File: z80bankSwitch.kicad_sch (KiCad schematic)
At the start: 27 parts, among them J1 Conn_02x05_Odd_Even, P101 CONN_01X04, P102 CONN_02X20, U1 SST39SF040, U101 7400, U102 Z8400, U105 74LS138, U2 AS6C4008-55PCN, Y101 4MHz

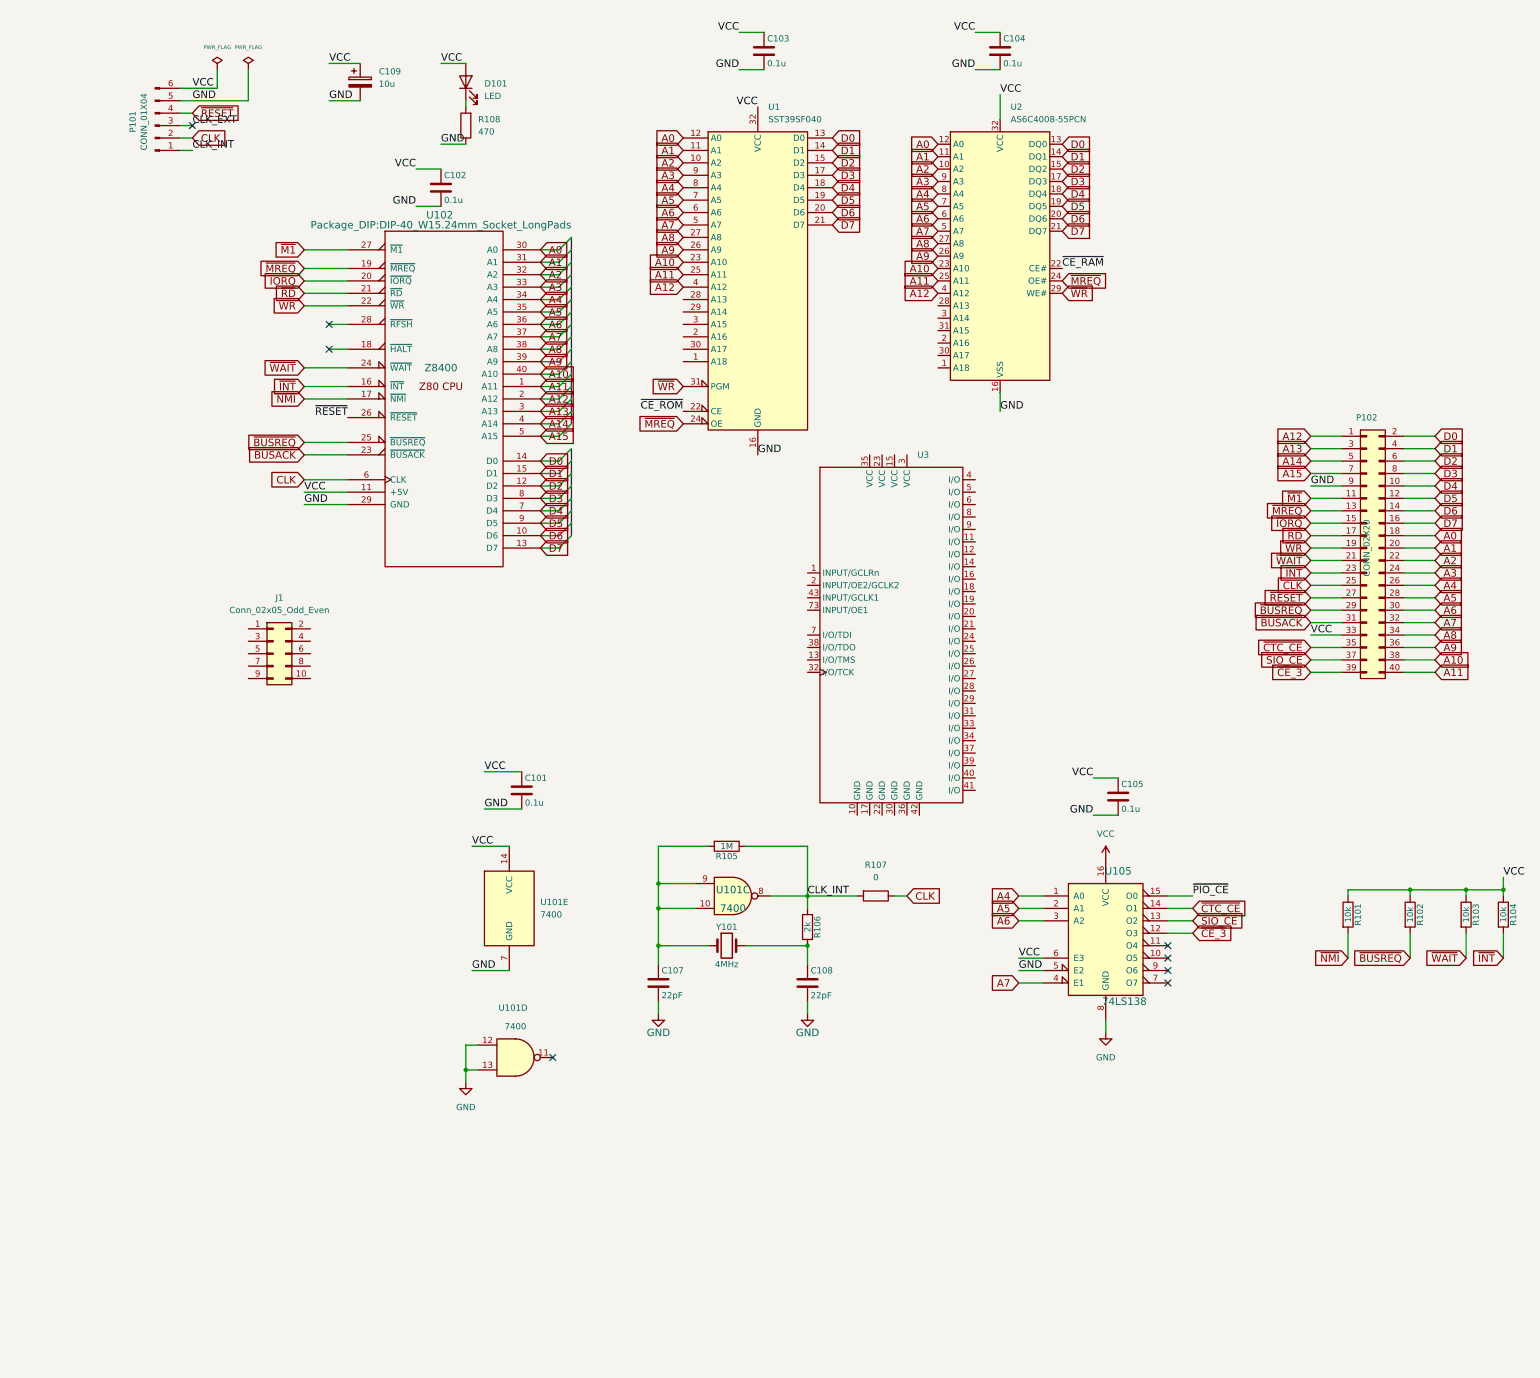
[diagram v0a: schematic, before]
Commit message: Use Z80 from global own library instead
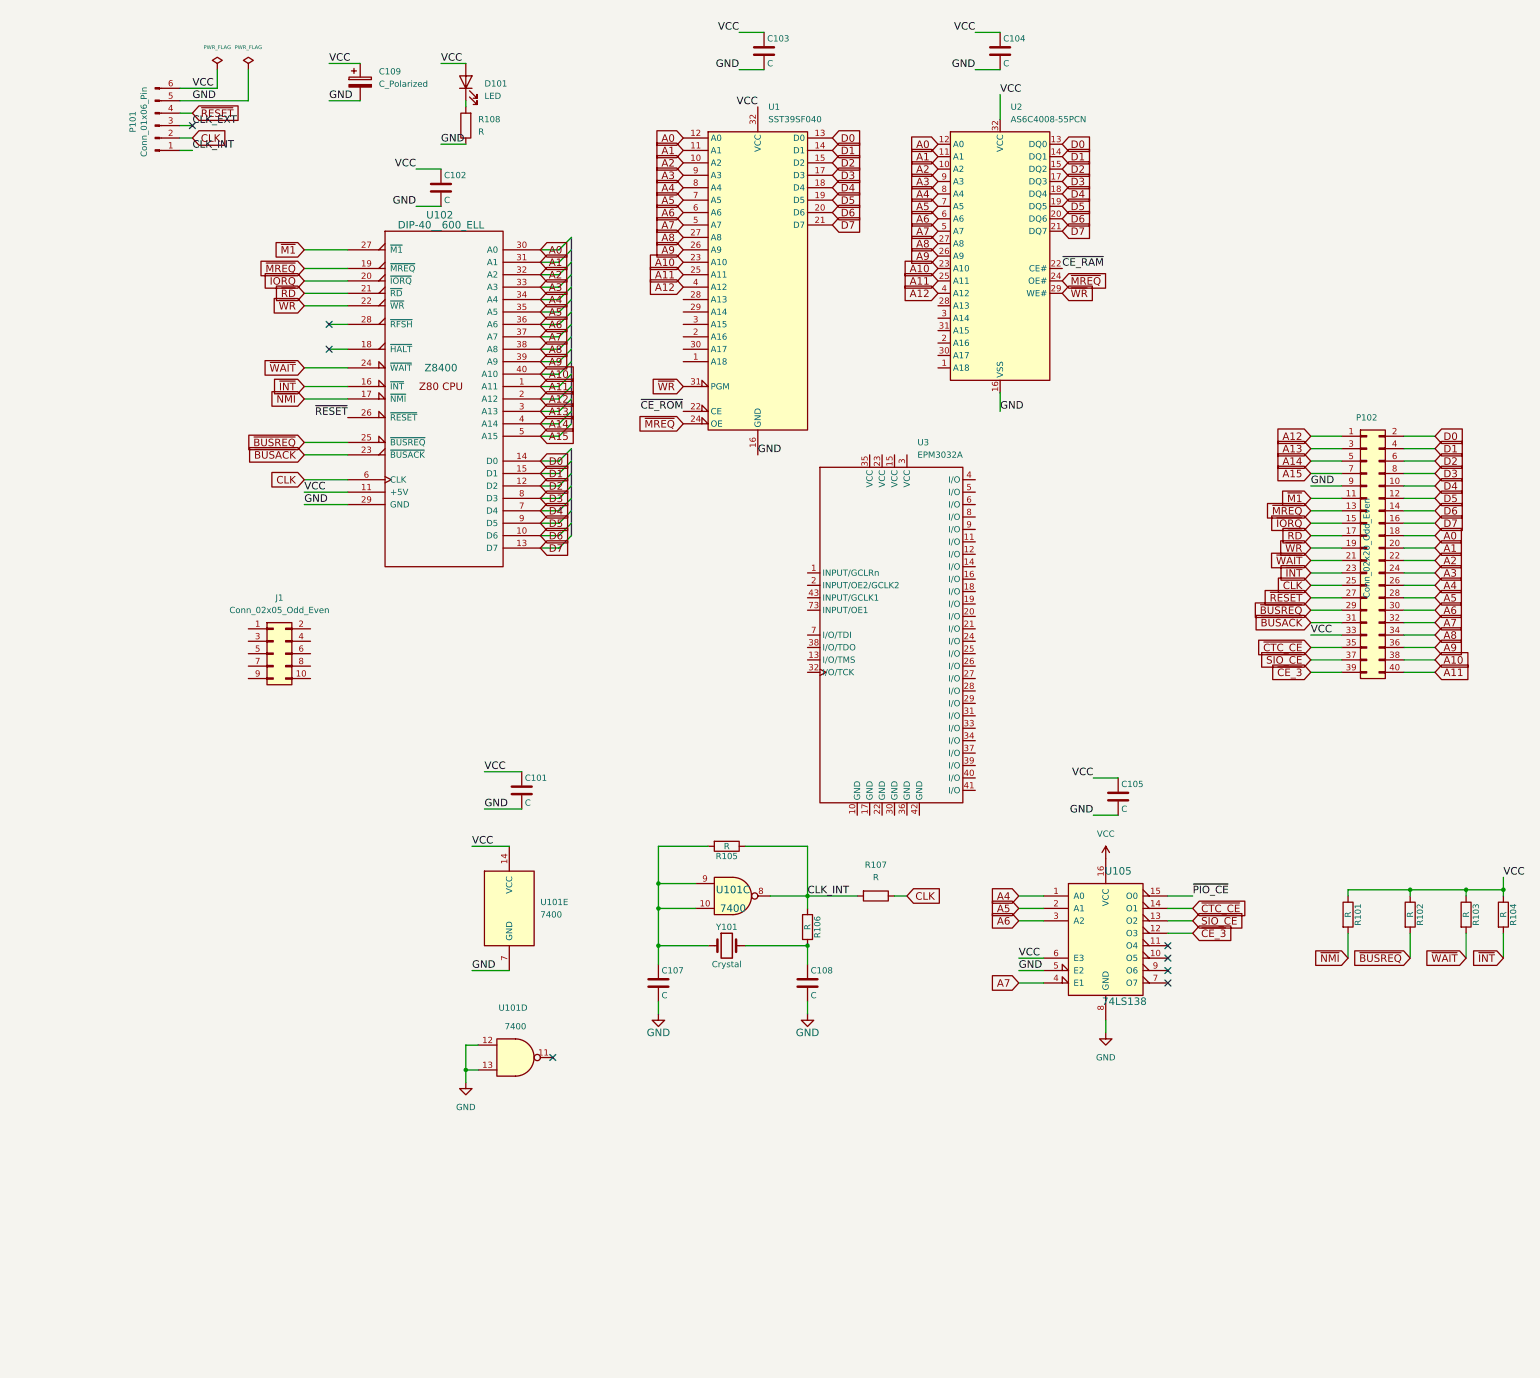
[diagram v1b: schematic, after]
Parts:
- C101, C102, C103, C104, C105: value 0.1u -> C
- C107, C108: value 22pF -> C
- C109: value 10u -> C_Polarized
- P101: value CONN_01X04 -> Conn_01x06_Pin
- P102: value CONN_02X20 -> Conn_02x20_Odd_Even
- R101, R102, R103, R104: value 10k -> R
- R105: value 1M -> R
- R106: value 2k -> R
- R107: value 0 -> R
- R108: value 470 -> R
- U102: footprint Package_DIP:DIP-40_W15.24mm_Socket_LongPads -> DIP-40__600_ELL; symbol z80-ownSymbols:Z8400 -> Own Symbol Library:Z8400
- U2: footprint Package_SO:TSOP-I-32_18.4x8mm_P0.5mm -> Package_DIP:DIP-32_W15.24mm
- U3: value (none) -> EPM3032A
- Y101: value 4MHz -> Crystal
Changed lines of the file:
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@@
 	)
 	(symbol
-		(lib_id "z80-ownSymbols:Z8400")
+		(lib_id "Own Symbol Library:Z8400")
 		(at 102.87 92.71 0)
 		(unit 1)
@@
 			)
 		)
-		(property "Footprint" "Package_DIP:DIP-40_W15.24mm_Socket_LongPads"
+		(property "Footprint" "DIP-40__600_ELL"
 			(at 101.6 58.42 0)
 			(show_name no)
@@
 		)
 		(instances
-			(project "z80"
+			(project "z80bankSwitch"
 				(path "/e7eeb274-d662-49f9-a7ce-d4911c9f2b64"
 					(reference "U102")
@@
 		)
 		(instances
-			(project "z80"
+			(project "z80bankSwitch"
 				(path "/e7eeb274-d662-49f9-a7ce-d4911c9f2b64"
 					(reference "U105")
@@
 			)
 		)
-		(property "Value" "CONN_01X04"
+		(property "Value" "Conn_01x06_Pin"
 			(at 40.894 37.338 90)
 			(show_name no)
@@
 		)
 		(instances
-			(project "z80"
+			(project "z80bankSwitch"
 				(path "/e7eeb274-d662-49f9-a7ce-d4911c9f2b64"
 					(reference "P101")
@@
 		)
 		(instances
-			(project "z80"
+			(project "z80bankSwitch"
 				(path "/e7eeb274-d662-49f9-a7ce-d4911c9f2b64"
 					(reference "#FLG0101")
@@
 		)
 		(instances
-			(project "z80"
+			(project "z80bankSwitch"
 				(path "/e7eeb274-d662-49f9-a7ce-d4911c9f2b64"
 					(reference "#FLG0102")
@@
 			)
 		)
-		(property "Value" "CONN_02X20"
+		(property "Value" "Conn_02x20_Odd_Even"
 			(at 290.83 124.46 90)
 			(show_name no)
@@
 		)
 		(instances
-			(project "z80"
+			(project "z80bankSwitch"
 				(path "/e7eeb274-d662-49f9-a7ce-d4911c9f2b64"
 					(reference "P102")
@@
 			)
 		)
-		(property "Value" "10k"
+		(property "Value" "R"
 			(at 318.77 199.39 90)
 			(show_name no)
@@
 		)
 		(instances
-			(project "z80"
+			(project "z80bankSwitch"
 				(path "/e7eeb274-d662-49f9-a7ce-d4911c9f2b64"
 					(reference "R104")
@@
 			)
 		)
-		(property "Value" "0.1u"
+		(property "Value" "C"
 			(at 118.745 176.53 0)
 			(show_name no)
@@
 		)
 		(instances
-			(project "z80"
+			(project "z80bankSwitch"
 				(path "/e7eeb274-d662-49f9-a7ce-d4911c9f2b64"
 					(reference "C101")
@@
 			)
 		)
-		(property "Value" "0.1u"
+		(property "Value" "C"
 			(at 102.235 53.34 0)
 			(show_name no)
@@
 		)
 		(instances
-			(project "z80"
+			(project "z80bankSwitch"
 				(path "/e7eeb274-d662-49f9-a7ce-d4911c9f2b64"
 					(reference "C102")
@@
 			)
 		)
-		(property "Value" "0.1u"
+		(property "Value" "C"
 			(at 168.275 25.4 0)
 			(show_name no)
@@
 		)
 		(instances
-			(project "z80"
+			(project "z80bankSwitch"
 				(path "/e7eeb274-d662-49f9-a7ce-d4911c9f2b64"
 					(reference "C103")
@@
 			)
 		)
-		(property "Value" "0.1u"
+		(property "Value" "C"
 			(at 216.535 25.4 0)
 			(show_name no)
@@
 		)
 		(instances
-			(project "z80"
+			(project "z80bankSwitch"
 				(path "/e7eeb274-d662-49f9-a7ce-d4911c9f2b64"
 					(reference "C104")
@@
 			)
 		)
-		(property "Value" "0.1u"
+		(property "Value" "C"
 			(at 240.665 177.8 0)
 			(show_name no)
@@
 		)
 		(instances
-			(project "z80"
+			(project "z80bankSwitch"
 				(path "/e7eeb274-d662-49f9-a7ce-d4911c9f2b64"
 					(reference "C105")
@@
 		)
 		(instances
-			(project "z80"
+			(project "z80bankSwitch"
 				(path "/e7eeb274-d662-49f9-a7ce-d4911c9f2b64"
 					(reference "U101")
@@
 			)
 		)
-		(property "Value" "2k"
+		(property "Value" "R"
 			(at 176.53 201.93 90)
 			(show_name no)
@@
 		)
 		(instances
-			(project "z80"
+			(project "z80bankSwitch"
 				(path "/e7eeb274-d662-49f9-a7ce-d4911c9f2b64"
 					(reference "R106")
@@
 			)
 		)
-		(property "Value" "22pF"
+		(property "Value" "C"
 			(at 177.165 215.9 0)
 			(show_name no)
@@
 		)
 		(instances
-			(project "z80"
+			(project "z80bankSwitch"
 				(path "/e7eeb274-d662-49f9-a7ce-d4911c9f2b64"
 					(reference "C108")
@@
 			)
 		)
-		(property "Value" "22pF"
+		(property "Value" "C"
 			(at 146.685 215.9 0)
 			(show_name no)
@@
 		)
 		(instances
-			(project "z80"
+			(project "z80bankSwitch"
 				(path "/e7eeb274-d662-49f9-a7ce-d4911c9f2b64"
 					(reference "C107")
@@
 			)
 		)
-		(property "Value" "4MHz"
+		(property "Value" "Crystal"
 			(at 160.02 209.55 0)
 			(show_name no)
@@
 		)
 		(instances
-			(project "z80"
+			(project "z80bankSwitch"
 				(path "/e7eeb274-d662-49f9-a7ce-d4911c9f2b64"
 					(reference "Y101")
@@
 			)
 		)
-		(property "Value" "1M"
+		(property "Value" "R"
 			(at 160.02 185.42 90)
 			(show_name no)
@@
 		)
 		(instances
-			(project "z80"
+			(project "z80bankSwitch"
 				(path "/e7eeb274-d662-49f9-a7ce-d4911c9f2b64"
 					(reference "R105")
@@
 		)
 		(instances
-			(project "z80"
+			(project "z80bankSwitch"
 				(path "/e7eeb274-d662-49f9-a7ce-d4911c9f2b64"
 					(reference "#PWR0102")
@@
 		)
 		(instances
-			(project "z80"
+			(project "z80bankSwitch"
 				(path "/e7eeb274-d662-49f9-a7ce-d4911c9f2b64"
 					(reference "#PWR0101")
@@
 		)
 		(instances
-			(project "z80"
+			(project "z80bankSwitch"
 				(path "/e7eeb274-d662-49f9-a7ce-d4911c9f2b64"
 					(reference "#PWR0105")
@@
 			)
 		)
-		(property "Value" "0"
+		(property "Value" "R"
 			(at 190.5 191.77 90)
 			(show_name no)
@@
 		)
 		(instances
-			(project "z80"
+			(project "z80bankSwitch"
 				(path "/e7eeb274-d662-49f9-a7ce-d4911c9f2b64"
 					(reference "R107")
@@
 		)
 		(instances
-			(project "z80"
+			(project "z80bankSwitch"
 				(path "/e7eeb274-d662-49f9-a7ce-d4911c9f2b64"
 					(reference "#PWR0104")
@@
 		)
 		(instances
-			(project "z80"
+			(project "z80bankSwitch"
 				(path "/e7eeb274-d662-49f9-a7ce-d4911c9f2b64"
 					(reference "U101")
@@
 		)
 		(instances
-			(project "z80"
+			(project "z80bankSwitch"
 				(path "/e7eeb274-d662-49f9-a7ce-d4911c9f2b64"
 					(reference "U1")
@@
 		(fields_autoplaced yes)
 		(property "Reference" "U3"
-			(at 198.9933 105.41 0)
+			(at 198.9933 102.87 0)
 			(show_name no)
 			(do_not_autoplace no)
@@
 			)
 		)
-		(property "Value" ""
-			(at 193.04 138.43 0)
+		(property "Value" "EPM3032A"
+			(at 198.9933 105.41 0)
 			(show_name no)
 			(do_not_autoplace no)
@@
 					(size 1.27 1.27)
 				)
+				(justify left)
 			)
 		)
@@
 		)
 		(instances
-			(project "z80"
+			(project "z80bankSwitch"
 				(path "/e7eeb274-d662-49f9-a7ce-d4911c9f2b64"
 					(reference "U3")
@@
 		)
 		(instances
-			(project "z80"
+			(project "z80bankSwitch"
 				(path "/e7eeb274-d662-49f9-a7ce-d4911c9f2b64"
 					(reference "J1")
@@
 			)
 		)
-		(property "Value" "10u"
+		(property "Value" "C_Polarized"
 			(at 88.9 29.5909 0)
 			(show_name no)
@@
 		)
 		(instances
-			(project "z80"
+			(project "z80bankSwitch"
 				(path "/e7eeb274-d662-49f9-a7ce-d4911c9f2b64"
 					(reference "C109")
@@
 		)
 		(instances
-			(project "z80"
+			(project "z80bankSwitch"
 				(path "/e7eeb274-d662-49f9-a7ce-d4911c9f2b64"
 					(reference "#PWR0103")
@@
 			)
 		)
-		(property "Value" "10k"
+		(property "Value" "R"
 			(at 311.15 199.39 90)
 			(show_name no)
@@
 		)
 		(instances
-			(project "z80"
+			(project "z80bankSwitch"
 				(path "/e7eeb274-d662-49f9-a7ce-d4911c9f2b64"
 					(reference "R103")
@@
 		)
 		(instances
-			(project "z80"
+			(project "z80bankSwitch"
 				(path "/e7eeb274-d662-49f9-a7ce-d4911c9f2b64"
 					(reference "U101")
@@
 		)
 		(instances
-			(project "z80"
+			(project "z80bankSwitch"
 				(path "/e7eeb274-d662-49f9-a7ce-d4911c9f2b64"
 					(reference "D101")
@@
 			)
 		)
-		(property "Value" "10k"
+		(property "Value" "R"
 			(at 287.02 199.39 90)
 			(show_name no)
@@
 		)
 		(instances
-			(project "z80"
+			(project "z80bankSwitch"
 				(path "/e7eeb274-d662-49f9-a7ce-d4911c9f2b64"
 					(reference "R101")
@@
 			)
 		)
-		(property "Value" "10k"
+		(property "Value" "R"
 			(at 299.72 199.39 90)
 			(show_name no)
@@
 		)
 		(instances
-			(project "z80"
+			(project "z80bankSwitch"
 				(path "/e7eeb274-d662-49f9-a7ce-d4911c9f2b64"
 					(reference "R102")
@@
 			)
 		)
-		(property "Value" "470"
+		(property "Value" "R"
 			(at 109.22 39.3699 0)
 			(show_name no)
@@
 		)
 		(instances
-			(project "z80"
+			(project "z80bankSwitch"
 				(path "/e7eeb274-d662-49f9-a7ce-d4911c9f2b64"
 					(reference "R108")
@@
 			)
 		)
-		(property "Footprint" "Package_SO:TSOP-I-32_18.4x8mm_P0.5mm"
+		(property "Footprint" "Package_DIP:DIP-32_W15.24mm"
 			(at 215.9 62.23 0)
 			(hide yes)
@@
 		)
 		(instances
-			(project "z80"
+			(project "z80bankSwitch"
 				(path "/e7eeb274-d662-49f9-a7ce-d4911c9f2b64"
 					(reference "U2")

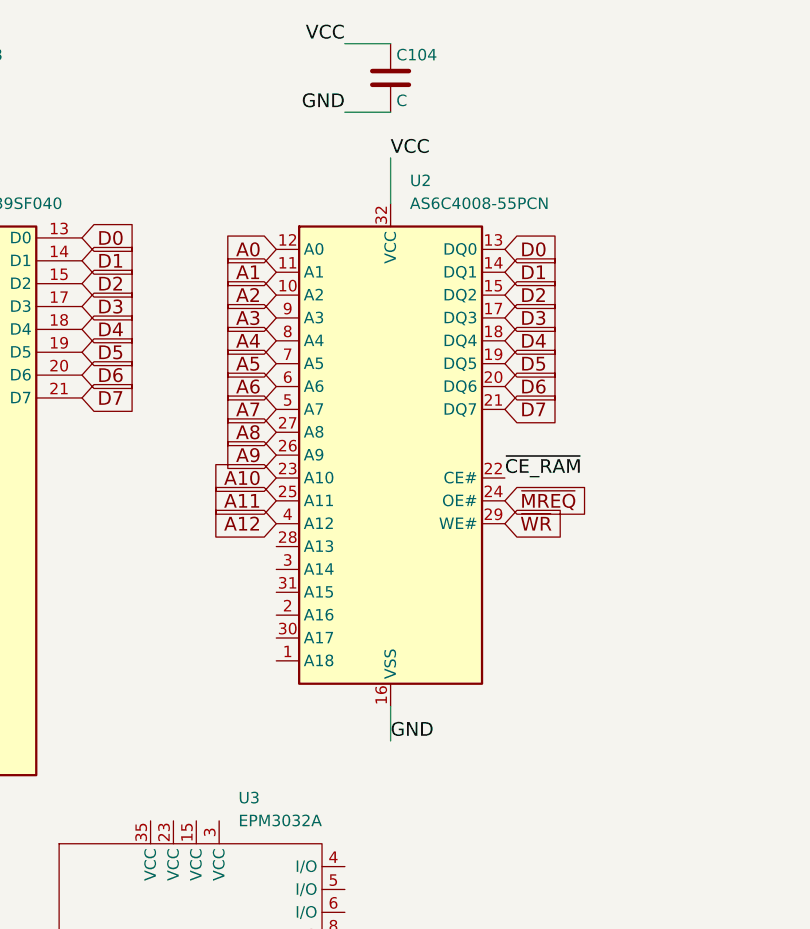
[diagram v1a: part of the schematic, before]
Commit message: Switch to 1Mx8 SRAM
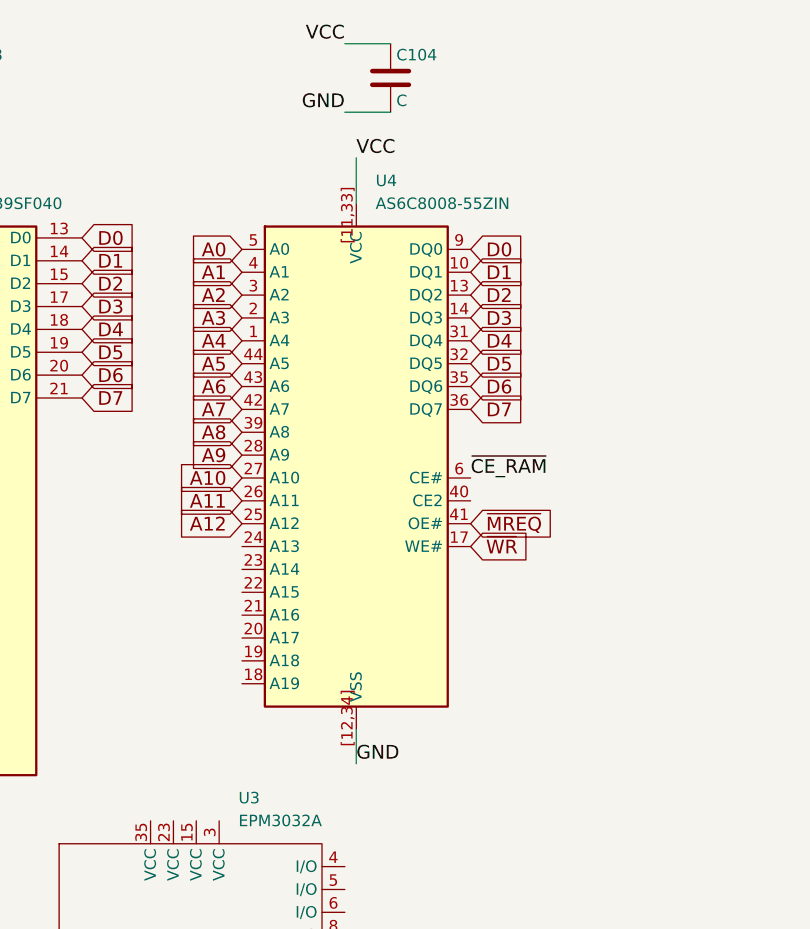
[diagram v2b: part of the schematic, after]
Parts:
- removed U2: AS6C4008-55PCN, Package_DIP:DIP-32_W15.24mm, symbol Memory_RAM:AS6C4008-55PCN
- added U4: AS6C8008-55ZIN, Package_SO:TSOP-II-44_10.16x18.41mm_P0.8mm, symbol Own Symbol Library:AS6C8008-55ZIN
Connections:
- net A0: now also U4.5 (A0)
- net A1: now also U4.4 (A1)
- net A10: now also U4.27 (A10)
- net A11: now also U4.26 (A11)
- net A12: now also U4.25 (A12)
- net A2: now also U4.3 (A2)
- net A3: now also U4.2 (A3)
- net A4: now also U4.1 (A4)
- net A5: now also U4.44 (A5)
- net A6: now also U4.43 (A6)
- net A7: now also U4.42 (A7)
- net A8: now also U4.39 (A8)
- net A9: now also U4.28 (A9)
- net D0: now also U4.9 (DQ0)
- net D1: now also U4.10 (DQ1)
- net D2: now also U4.13 (DQ2)
- net D3: now also U4.14 (DQ3)
- net D4: now also U4.31 (DQ4)
- net D5: now also U4.32 (DQ5)
- net D6: now also U4.35 (DQ6)
- net D7: now also U4.36 (DQ7)
- net GND: now also U4.[12,34] (VSS)
- net VCC: now also U4.[11,33] (VCC)
- net ~{CE_RAM}: now also U4.6 (CE#)
- net ~{MREQ}: now also U4.41 (OE#)
- net ~{WR}: now also U4.17 (WE#)
